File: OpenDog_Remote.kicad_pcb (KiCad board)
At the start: 2 copper layers, 81 x 51 mm, 37 parts, among them J1 Conn_01x03_Pin, J10 Conn_01x03_Pin, J11 Conn_01x03_Pin, J12 Conn_01x02_Pin, J13 Conn_01x03_Pin, J14 Conn_01x03_Pin, J15 Conn_01x03_Pin, J16 Conn_01x03_Pin, J17 NRF, J18 Conn_02x08_Odd_Even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

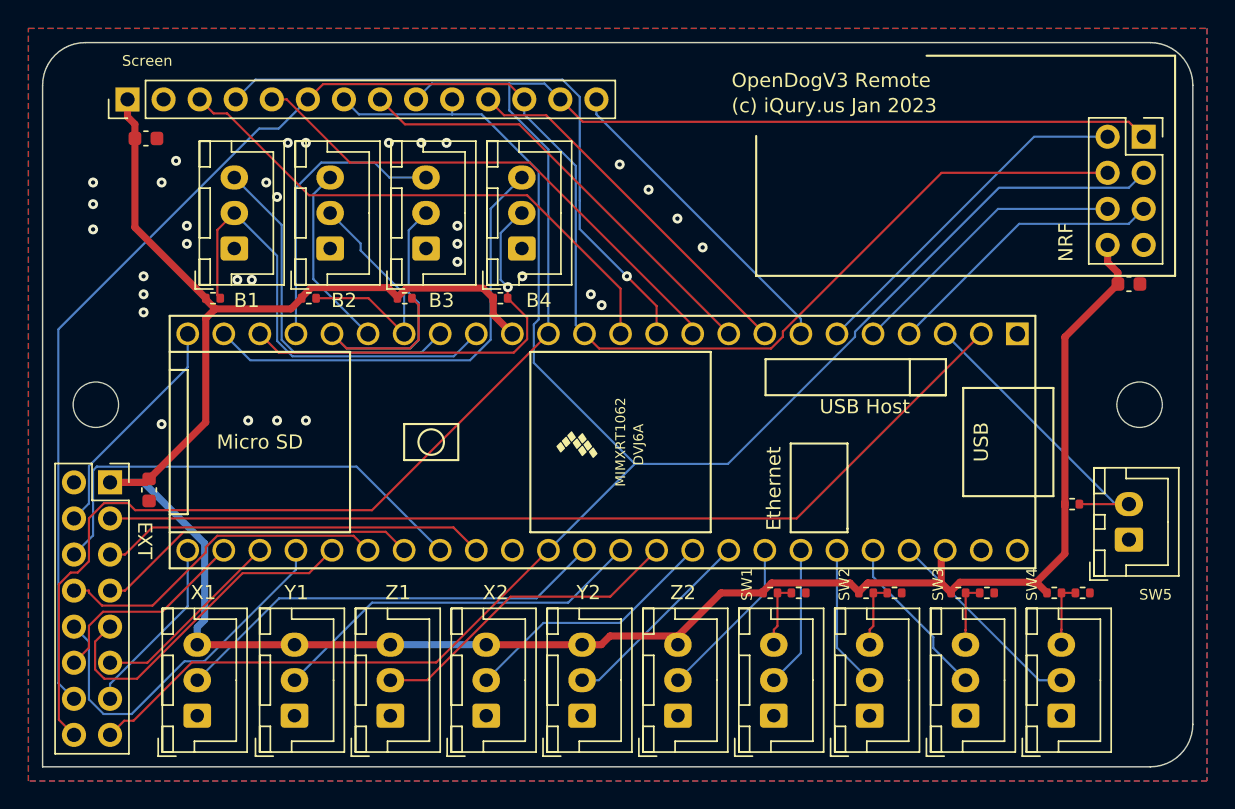
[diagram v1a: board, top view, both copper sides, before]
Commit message: Update the OpenDog remote board.
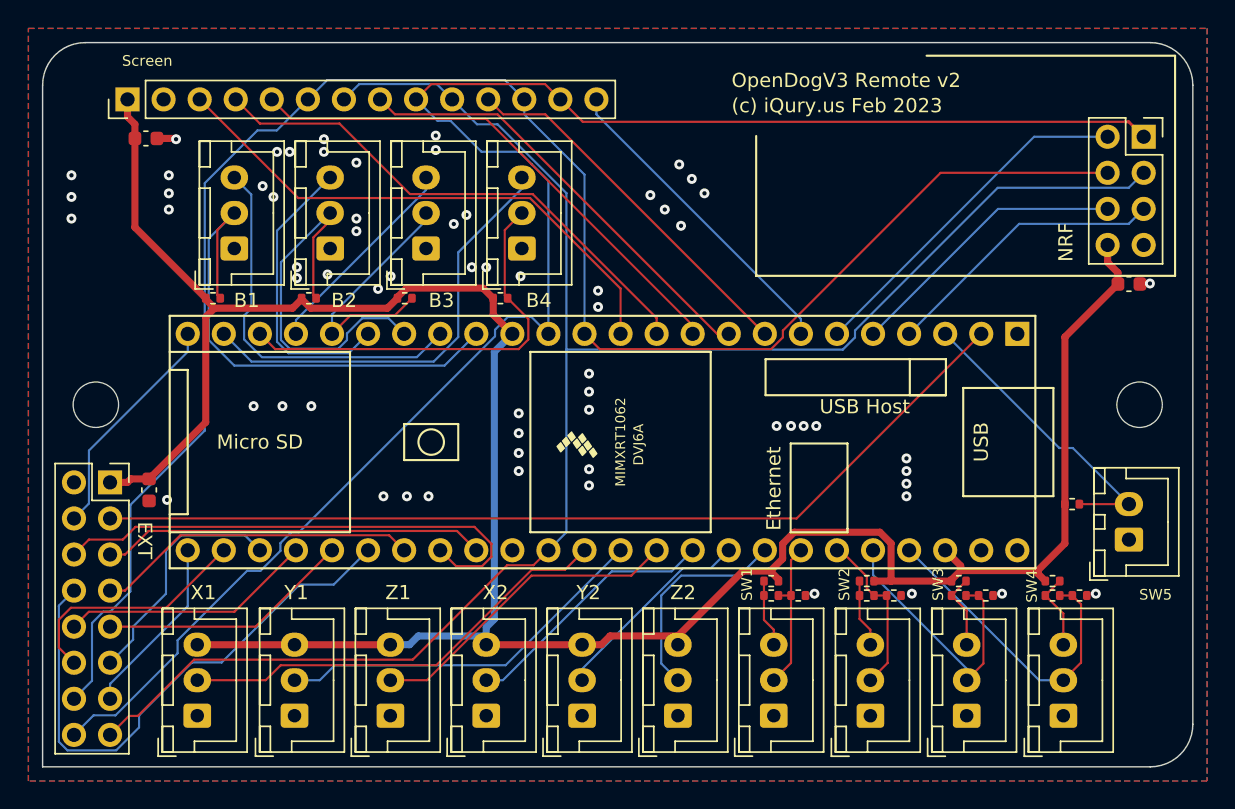
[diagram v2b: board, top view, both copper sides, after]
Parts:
- added R14: 10k, Resistor_SMD:R_0402_1005Metric, F.Cu at (131.1, 88.9)
- added R15: 10k, Resistor_SMD:R_0402_1005Metric, F.Cu at (133.0, 88.9)
- added R16: 10k, Resistor_SMD:R_0402_1005Metric, F.Cu at (131.1, 87.9)
- added R17: 10k, Resistor_SMD:R_0402_1005Metric, F.Cu at (111.3, 87.9)
- moved R8 8.76 mm to (124.5, 87.9)
- moved R5 6.50 mm to (118.0, 87.9), turned to 180 degrees
- moved R7 4.82 mm to (126.4, 88.9)
- moved R6 1.99 mm to (124.5, 88.9)
- moved R1 0.20 mm to (111.3, 88.9)
- moved R3 0.19 mm to (118.0, 88.9)
- moved R4 0.19 mm to (119.9, 88.9)
- moved R2 0.19 mm to (113.2, 88.9)
- moved J11 0.14 mm to (131.9, 97.4)
- moved J10 0.08 mm to (125.1, 97.4)
- moved J9 0.05 mm to (118.3, 97.4)
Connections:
- R1 pad 1: /3.3V -> Net-(J8-Pin_3)
- R1 pad 2: Net-(J8-Pin_3) -> /SW1
- R2 pad 1: Net-(J8-Pin_3) -> /SW1
- R3 pad 1: /3.3V -> Net-(J9-Pin_3)
- R3 pad 2: Net-(J9-Pin_3) -> /SW2
- R4 pad 1: Net-(J9-Pin_3) -> /SW2
- R5 pad 2: Net-(J10-Pin_3) -> Net-(J9-Pin_3)
- R6 pad 2: GND -> /SW3
- R7 pad 1: /3.3V -> /SW3
- R7 pad 2: Net-(J11-Pin_3) -> GND
- R8 pad 1: Net-(J11-Pin_3) -> /3.3V
- R8 pad 2: GND -> Net-(J10-Pin_3)
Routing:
- net /EX6: track 23.9 -> 39.4 mm
- net /3.3V: track 166.8 -> 178.7 mm
- net /B2: track 17.9 -> 27.5 mm
- net /B3: track 26.4 -> 17.9 mm
- net /EX8: track 26.1 -> 17.9 mm
- net /SW4: track 14.5 -> 22.3 mm
- net /SW3: track 11.8 -> 19.4 mm
- net /B2_LED: track 13.1 -> 20.4 mm
- net /RESET: track 44.2 -> 37.1 mm, vias 1 -> 0
- net /EX7: track 24.2 -> 17.9 mm
- net /B3_LED: track 20.6 -> 14.8 mm
- net /B1: track 32.0 -> 36.8 mm
- net /MISO: track 127.0 -> 122.9 mm
- net /Z2: track 11.7 -> 15.1 mm
- net /EX9: track 13.8 -> 17.0 mm
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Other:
- board text added: "(c) iQury.us Feb 2023"
- board text added: "OpenDogV3 Remote v2"
- board text removed: "(c) iQury.us Jan 2023"
- board text removed: "OpenDogV3 Remote"

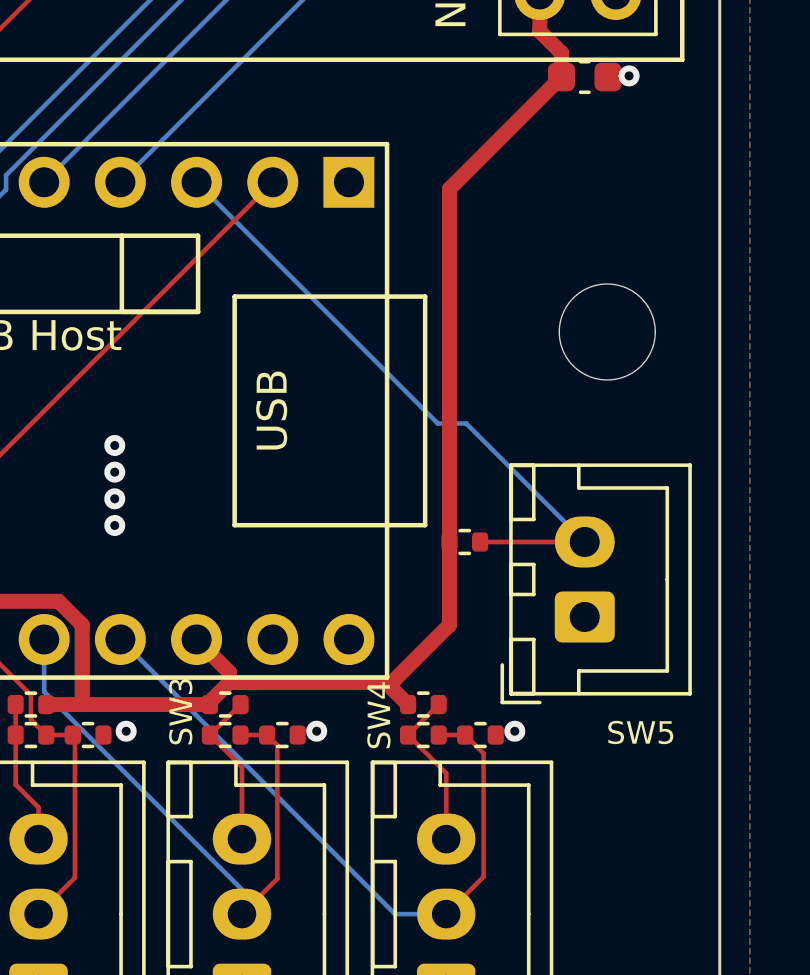
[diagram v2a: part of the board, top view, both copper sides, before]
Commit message: Move the SW5 connector away fromt he USB cable.
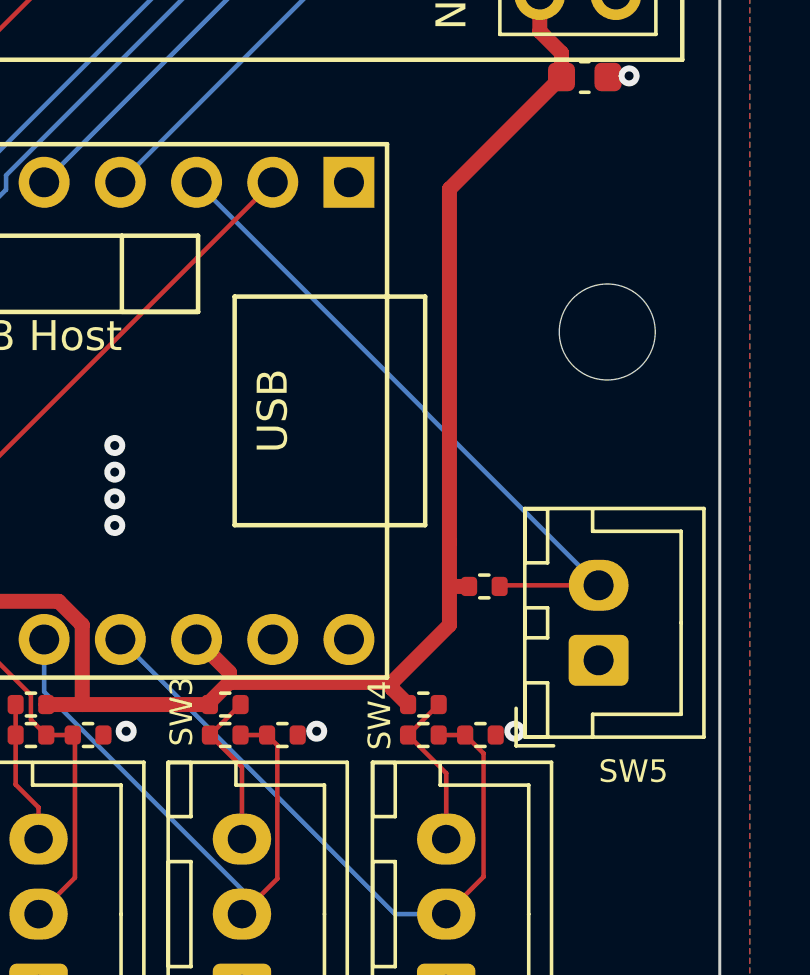
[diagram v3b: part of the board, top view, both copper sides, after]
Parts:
- moved R9 1.62 mm to (133.2, 84.0)
- moved J12 1.52 mm to (137.0, 86.4)
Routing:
- net /SW5: track 21.4 -> 22.3 mm
- net /3.3V: track 178.7 -> 179.4 mm
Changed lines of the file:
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@@
   )
   (footprint "Resistor_SMD:R_0402_1005Metric" (layer "F.Cu")
-    (at 132.5 82.5)
+    (at 133.152 83.982)
     (descr "Resistor SMD 0402 (1005 Metric), square (rectangular) end terminal, IPC_7351 nominal, (Body size source: IPC-SM-782 page 72, https://www.pcb-3d.com/wordpress/wp-content/uploads/ipc-sm-782a_amendment_1_and_2.pdf), generated with kicad-footprint-generator")
     (tags "resistor")
@@
   )
   (footprint "Connector_JST:JST_XH_B2B-XH-A_1x02_P2.50mm_Vertical" (layer "F.Cu")
-    (at 136.5 85 90)
+    (at 136.962 86.444249 90)
     (descr "JST XH series connector, B2B-XH-A (http://www.jst-mfg.com/product/pdf/eng/eXH.pdf), generated with kicad-footprint-generator")
     (tags "connector JST XH vertical")
@@
     (effects (font (size 1 1) (thickness 0.15)) (justify left bottom mirror))
   )
-  (gr_text "LED" (at 90.734 60.36) (layer "B.SilkS")
-    (effects (font (size 1 1) (thickness 0.15)) (justify left bottom mirror))
-  )
   (gr_text "GND" (at 116.388 98.206) (layer "B.SilkS")
     (effects (font (size 1 1) (thickness 0.15)) (justify left bottom mirror))
@@
     (effects (font (size 1 1) (thickness 0.15)) (justify left bottom mirror))
   )
-  (gr_text "GND" (at 137.978 87.538) (layer "B.SilkS")
+  (gr_text "GND" (at 138.486 89.316) (layer "B.SilkS")
     (effects (font (size 1 1) (thickness 0.15)) (justify left bottom mirror))
   )
@@
     (effects (font (size 1 1) (thickness 0.15)) (justify left bottom))
   )
-  (gr_text "SW5" (at 137.216 89.316) (layer "F.SilkS")
+  (gr_text "SW5" (at 136.962 90.586) (layer "F.SilkS")
     (effects (font (size 0.75 0.75) (thickness 0.1)) (justify left bottom))
   )
@@
   (segment (start 109.3062 87.2201) (end 111.2435 87.2201) (width 0.5) (layer "F.Cu") (net 8))
   (segment (start 135.725 66.2023) (end 135.725 67) (width 0.5) (layer "F.Cu") (net 8))
-  (segment (start 131.99 82.5) (end 131.99 85.2669) (width 0.5) (layer "F.Cu") (net 8))
   (segment (start 131.99 85.2669) (end 130.0758 87.1811) (width 0.5) (layer "F.Cu") (net 8))
   (segment (start 135 64.25) (end 135 65.4773) (width 0.5) (layer "F.Cu") (net 8))
@@
   (segment (start 77.609 68.7013) (end 72.1084 68.7013) (width 0.5) (layer "F.Cu") (net 8))
   (segment (start 112.9283 84.4784) (end 112.1158 85.2909) (width 0.5) (layer "F.Cu") (net 8))
+  (segment (start 131.99 83.982) (end 131.99 85.2669) (width 0.5) (layer "F.Cu") (net 8))
   (segment (start 66.5 63.01) (end 71.49 68) (width 0.5) (layer "F.Cu") (net 8))
   (segment (start 91.0193 67.2893) (end 85.6253 67.2893) (width 0.5) (layer "F.Cu") (net 8))
@@
   (segment (start 130.0758 87.3848) (end 130.61 87.919) (width 0.5) (layer "F.Cu") (net 8))
   (segment (start 84.99 68) (end 84.2859 68.7041) (width 0.5) (layer "F.Cu") (net 8))
+  (segment (start 131.99 83.982) (end 132.642 83.982) (width 0.5) (layer "F.Cu") (net 8))
   (segment (start 124.6545 86.8445) (end 123.56 85.75) (width 0.5) (layer "F.Cu") (net 8))
   (segment (start 66.5 55.7473) (end 66.5 56.75) (width 0.5) (layer "F.Cu") (net 8))
@@
   (segment (start 119.75 87.919) (end 118.549 87.919) (width 0.5) (layer "F.Cu") (net 8))
   (segment (start 104.74 91.7863) (end 109.3062 87.2201) (width 0.5) (layer "F.Cu") (net 8))
+  (segment (start 131.99 82.5) (end 131.99 83.982) (width 0.5) (layer "F.Cu") (net 8))
   (segment (start 124.006 87.8296) (end 124.006 87.919) (width 0.5) (layer "F.Cu") (net 8))
   (segment (start 130.0758 87.1811) (end 130.0758 87.3848) (width 0.5) (layer "F.Cu") (net 8))
@@
   (segment (start 131.882 94.904) (end 130.174 94.904) (width 0.1524) (layer "B.Cu") (net 21))
   (segment (start 130.174 94.904) (end 121.02 85.75) (width 0.1524) (layer "B.Cu") (net 21))
-  (segment (start 136.5 82.5) (end 133.01 82.5) (width 0.1524) (layer "F.Cu") (net 22))
-  (segment (start 132.5495 78.5495) (end 136.5 82.5) (width 0.1524) (layer "B.Cu") (net 22))
-  (segment (start 131.5995 78.5495) (end 123.56 70.51) (width 0.1524) (layer "B.Cu") (net 22))
-  (segment (start 131.5995 78.5495) (end 132.5495 78.5495) (width 0.1524) (layer "B.Cu") (net 22))
+  (segment (start 133.662 83.982) (end 133.699751 83.944249) (width 0.1524) (layer "F.Cu") (net 22))
+  (segment (start 133.699751 83.944249) (end 136.962 83.944249) (width 0.1524) (layer "F.Cu") (net 22))
+  (segment (start 131.155 78.105) (end 131.155 78.137249) (width 0.1524) (layer "B.Cu") (net 22))
+  (segment (start 131.155 78.137249) (end 136.962 83.944249) (width 0.1524) (layer "B.Cu") (net 22))
+  (segment (start 131.155 78.105) (end 123.56 70.51) (width 0.1524) (layer "B.Cu") (net 22))
   (segment (start 72.3053 67.7953) (end 72.3053 63.1947) (width 0.1524) (layer "F.Cu") (net 23))
   (segment (start 72.3053 63.1947) (end 73.5 62) (width 0.1524) (layer "F.Cu") (net 23))

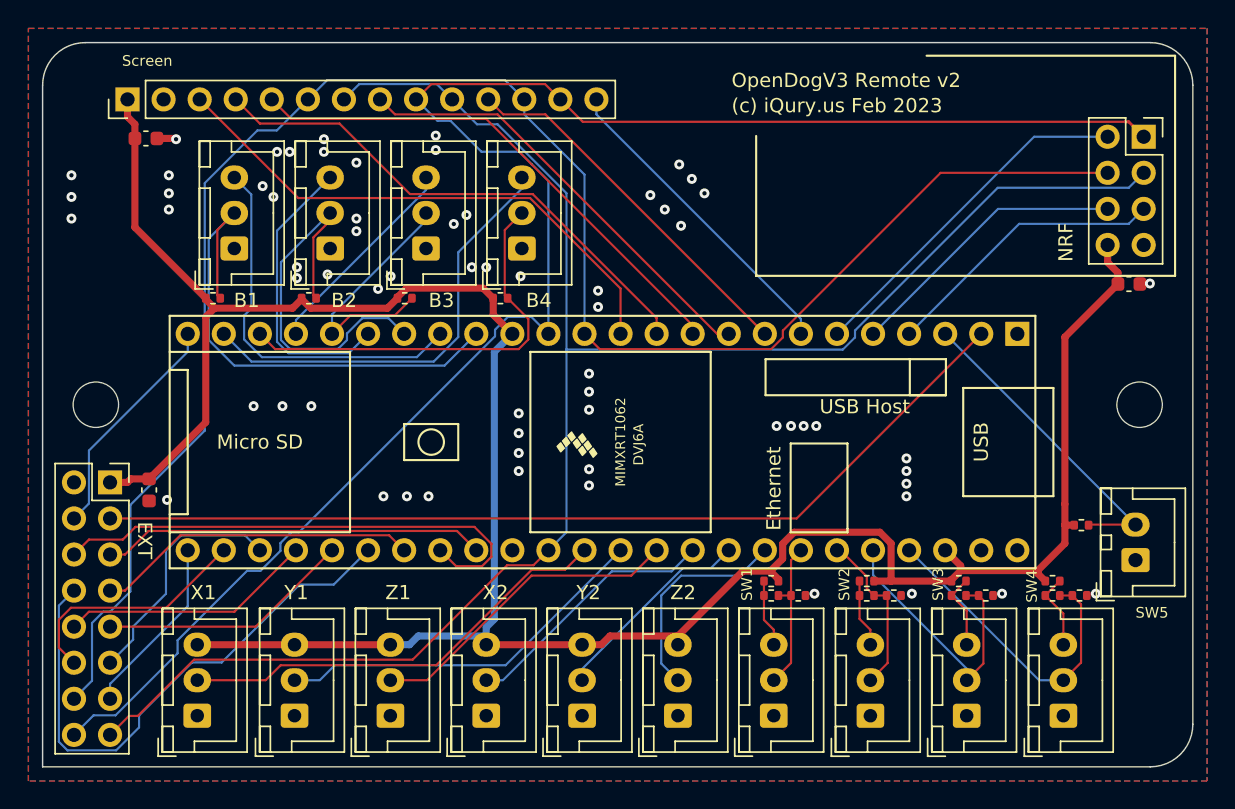
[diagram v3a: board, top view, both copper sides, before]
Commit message: Add filtering caps on the switches and pots.
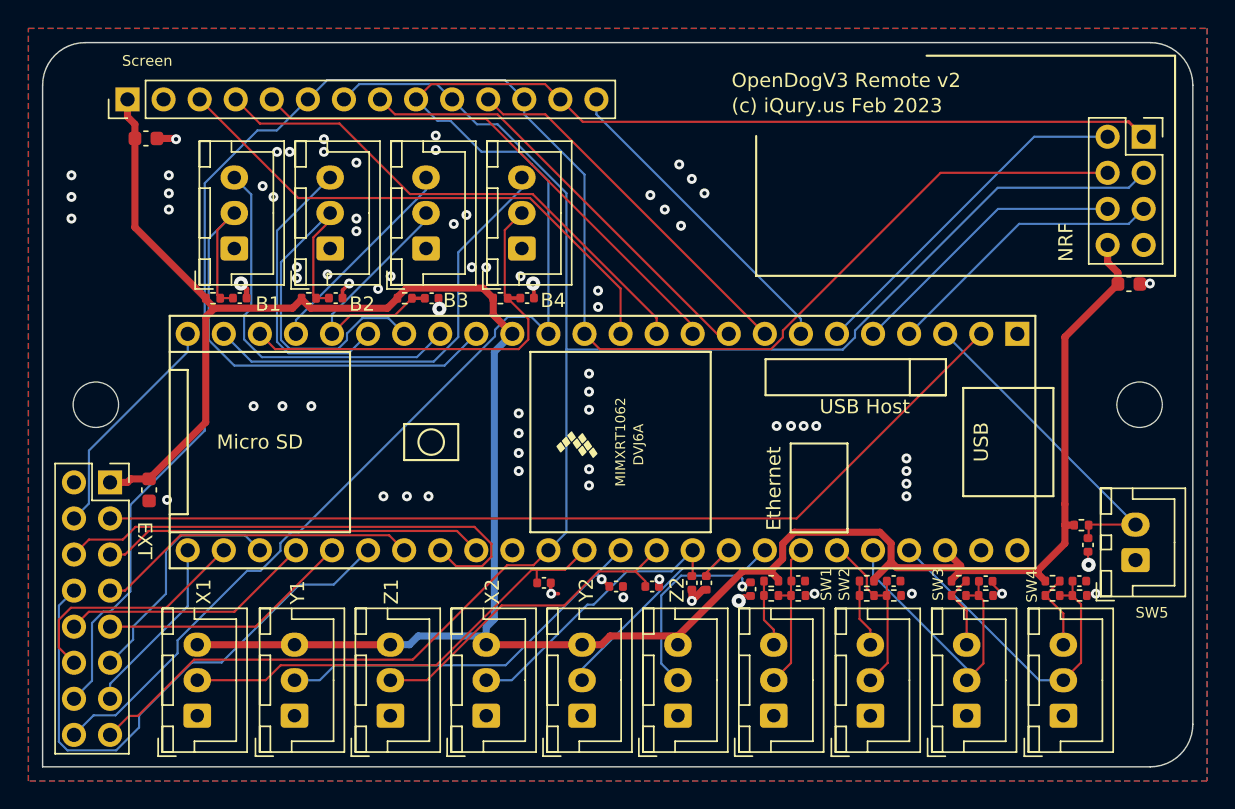
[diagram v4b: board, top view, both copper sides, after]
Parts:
- added C10: 1nF, Capacitor_SMD:C_0402_1005Metric, F.Cu at (94.1, 68.0)
- added C11: 1nF, Capacitor_SMD:C_0402_1005Metric, F.Cu at (87.4, 68.0)
- added C12: 1nF, Capacitor_SMD:C_0402_1005Metric, F.Cu at (80.6, 68.0)
- added C13: 1nF, Capacitor_SMD:C_0402_1005Metric, F.Cu at (73.9, 68.0)
- added C14: 1nF, Capacitor_SMD:C_0402_1005Metric, F.Cu at (113.2, 87.9)
- added C15: 1nF, Capacitor_SMD:C_0402_1005Metric, F.Cu at (119.9, 87.9)
- added C16: 1nF, Capacitor_SMD:C_0402_1005Metric, F.Cu at (126.4, 87.9)
- added C17: 1nF, Capacitor_SMD:C_0402_1005Metric, F.Cu at (133.0, 87.9)
- added C18: 1nF, Capacitor_SMD:C_0402_1005Metric, F.Cu at (133.6, 85.4)
- added C4: 1nF, Capacitor_SMD:C_0402_1005Metric, F.Cu at (95.3, 88.0)
- added C5: 1nF, Capacitor_SMD:C_0402_1005Metric, F.Cu at (100.4, 88.3)
- added C6: 1nF, Capacitor_SMD:C_0402_1005Metric, F.Cu at (102.9, 88.3)
- added C7: 1nF, Capacitor_SMD:C_0402_1005Metric, F.Cu at (105.7, 88.0)
- added C8: 1nF, Capacitor_SMD:C_0402_1005Metric, F.Cu at (106.7, 88.0)
- added C9: 1nF, Capacitor_SMD:C_0402_1005Metric, F.Cu at (109.8, 88.5)
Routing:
- net GND: track 1.37 -> 12.1 mm, vias 65 -> 75
- net /Y2: track 14.6 -> 17.1 mm
- net /X2: track 18.3 -> 20.2 mm
- net /Z2: track 15.1 -> 16.6 mm, vias 0 -> 1
- net /Z1: track 22.5 -> 23.9 mm
- net /Y1: track 26.8 -> 28.0 mm, vias 0 -> 1
- net /SW2: track 11.8 -> 12.8 mm
- net /SW4: track 22.3 -> 23.3 mm
- net /SW3: track 19.4 -> 20.4 mm
- net /SW5: track 22.3 -> 23.2 mm
- net /X1: track 31.1 -> 32.0 mm
- net /B3: track 17.9 -> 18.8 mm
- net /B2: track 27.5 -> 28.4 mm
- net /B1: track 36.8 -> 37.7 mm
- net /B4: track 29.7 -> 30.6 mm
